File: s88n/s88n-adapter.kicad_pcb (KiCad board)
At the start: 2 copper layers, 30 x 40 mm, 8 parts, among them J1 RJ45, P1 S88, P2 PWR, P3 Power

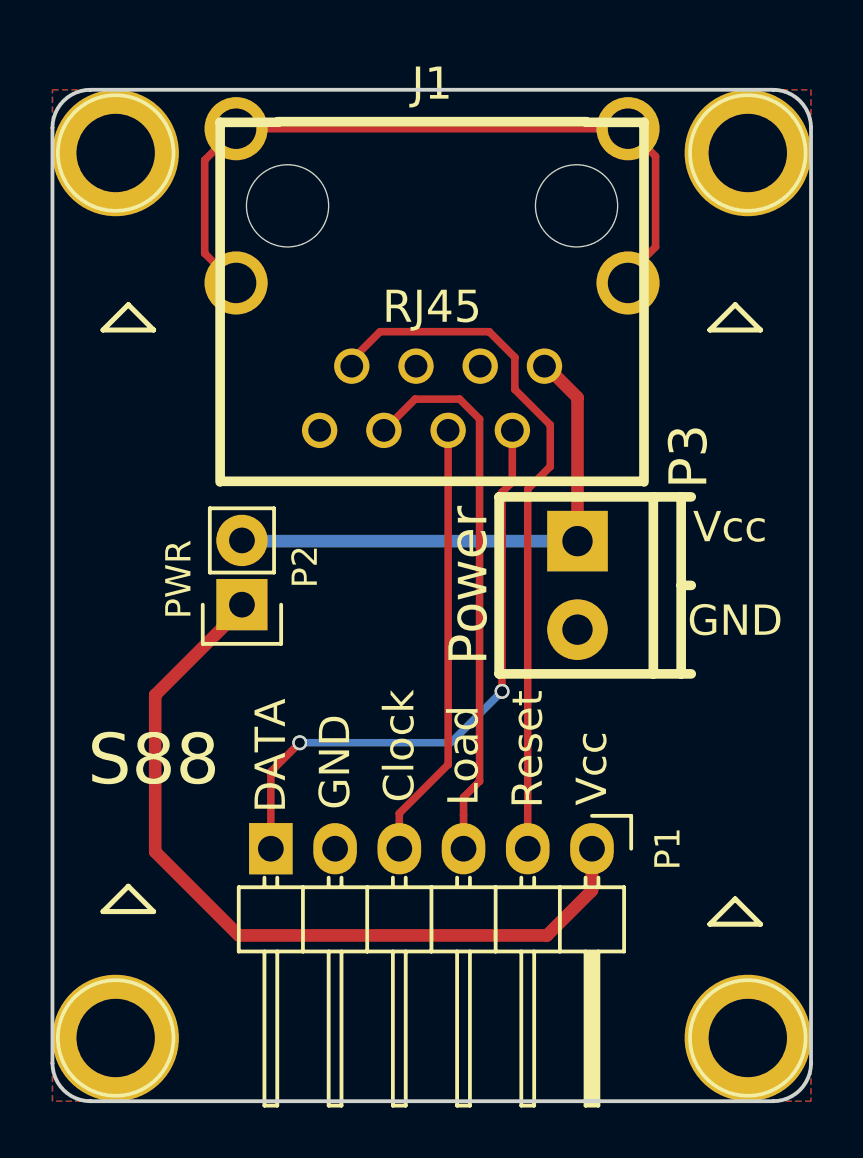
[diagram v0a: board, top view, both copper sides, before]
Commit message: add template
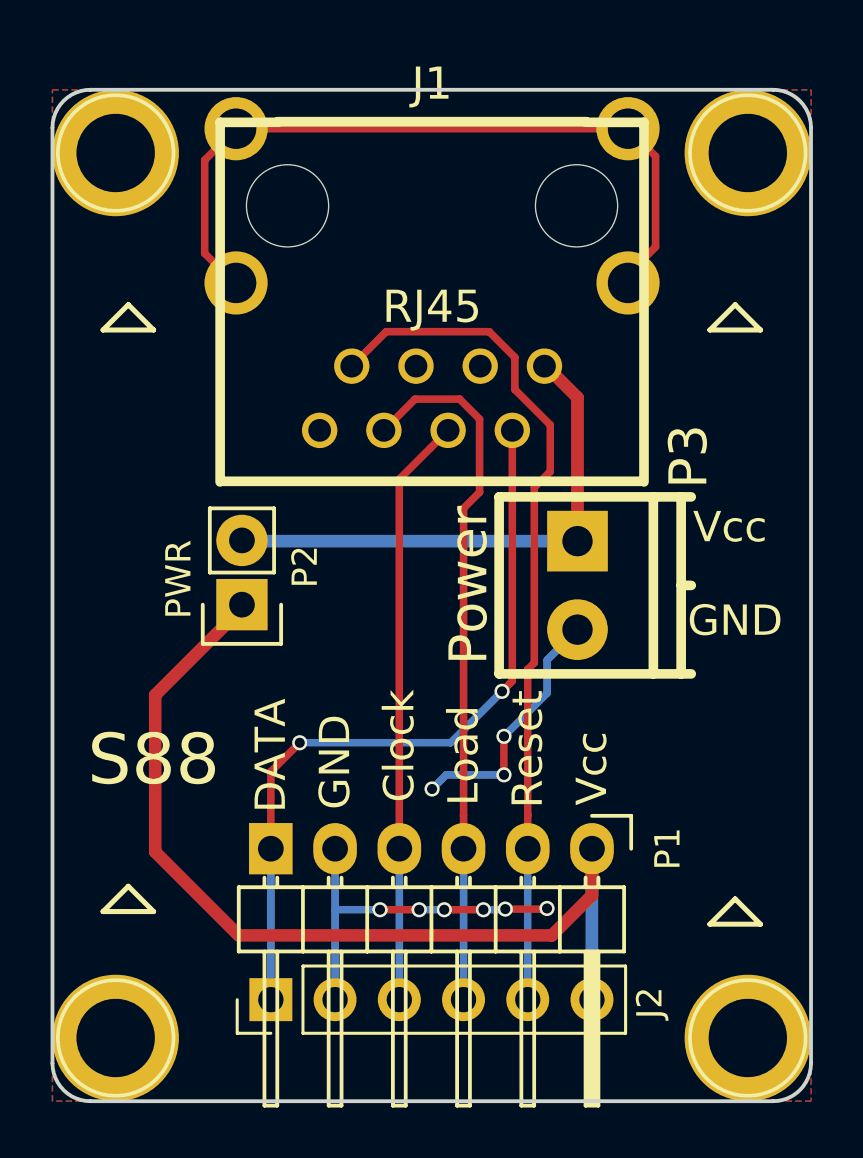
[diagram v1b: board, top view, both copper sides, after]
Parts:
- added J2: Conn_01x06, Pin_Headers:Pin_Header_Straight_1x06_Pitch2.54mm, F.Cu at (143.6, 126.0)
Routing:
- net /GND: track 0.02 -> 24.4 mm, vias 0 -> 9
- net /Vcc: track 32.1 -> 38.2 mm
- net /Load: track 21.9 -> 27.8 mm
- net /DATA: track 24.0 -> 30.0 mm
- net /Clock: track 17.3 -> 23.3 mm
- net /Reset: track 28.0 -> 33.8 mm
